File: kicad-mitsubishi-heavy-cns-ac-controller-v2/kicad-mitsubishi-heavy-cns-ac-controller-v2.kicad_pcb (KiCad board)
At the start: 2 copper layers, 42.7 x 48.8 mm, 31 parts, among them J3 USB_OTG, J4 Conn_01x05_Pin, SW1 SW_Push, SW2 SW_Push, U1 Si8641BB-B-IU, U2 AP2112K-3.3, U3 ESP32-C3-WROOM-02, U5 AOZ1282CI-1

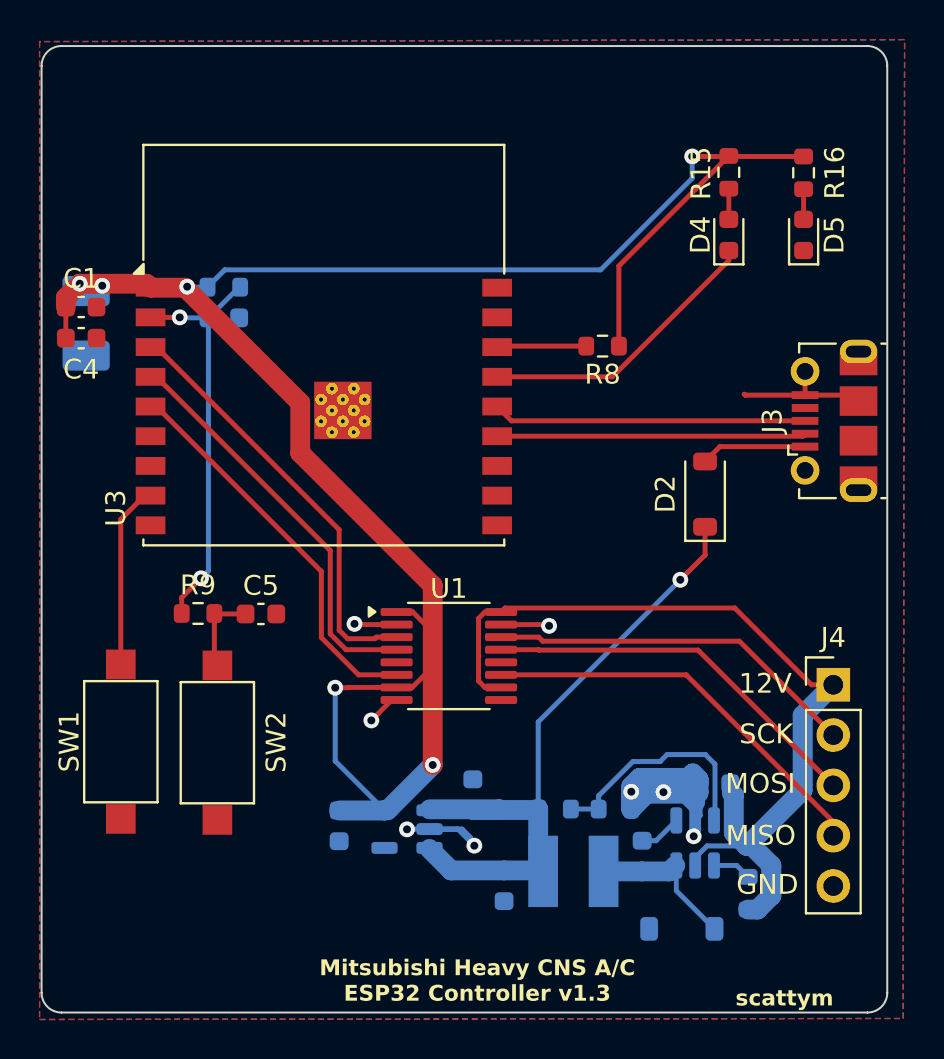
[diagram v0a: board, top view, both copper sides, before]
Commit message: First pcb design for the v2 board.
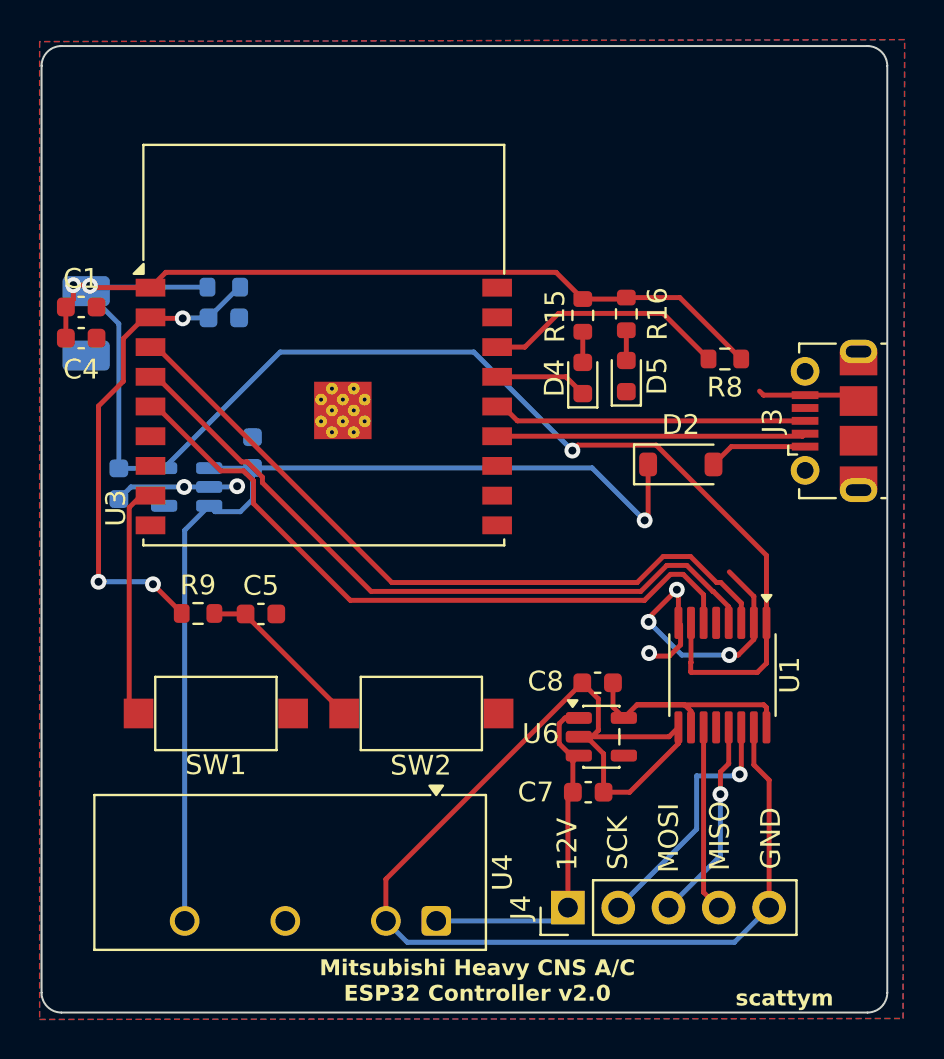
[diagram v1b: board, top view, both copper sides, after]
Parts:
- removed C9: 10uF X7R, Capacitor_SMD:C_0603_1608Metric
- removed D3: PMEG4005EGWX, Diode_SMD:D_SOD-123
- removed L1: 2.2uH, Inductor_SMD:L_Bourns-SRN4018
- removed R12: 49.9K, Resistor_SMD:R_0603_1608Metric
- removed R13: 15.8K, Resistor_SMD:R_0603_1608Metric
- removed R14: 10K, Resistor_SMD:R_0603_1608Metric
- removed U5: AOZ1282CI-1, Package_TO_SOT_SMD:SOT-23-6
- added U4: TBA2-1211, Converter_DCDC:Converter_DCDC_TRACO_TBA2-xxxx_Single_THT, F.Cu at (93.0, 90.2)
- added U6: AP2210K-5.0, Package_TO_SOT_SMD:SOT-23-5, F.Cu at (101.3, 80.9)
- C7: value 10uF X7R -> 1uF X7R; moved to F.Cu
- C8: value 0.1uF -> 2.2uF X7R; moved to F.Cu
- moved C10 20.5 mm to (76.9, 68.1)
- moved C6 20.5 mm to (83.7, 66.5)
- moved U2 20.5 mm to (80.3, 68.3)
- moved J4 17.5 mm to (99.6, 89.5), turned to 90 degrees
- moved U1 13.8 mm to (107.4, 77.8), turned to -90 degrees
- moved D5 11.4 mm to (102.5, 62.7)
- moved R16 11.4 mm to (102.5, 59.5)
- moved SW2 10.4 mm to (92.2, 79.7), turned to 180 degrees
- moved D4 10.3 mm to (100.3, 62.8)
- moved R15 10.3 mm to (100.3, 59.6)
- moved C8 9.03 mm to (101.1, 78.2), turned to 180 degrees
- moved C7 6.41 mm to (100.6, 83.7), turned to 0 degrees
- moved R8 6.21 mm to (107.5, 61.8)
- moved SW1 5.01 mm to (81.8, 79.7), turned to 180 degrees
- moved D2 1.94 mm to (105.3, 67.1), turned to 0 degrees
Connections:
- C1 pad 2: GND -> GND1
- C10 pad 2: GND -> GND1
- C2 pad 2: GND -> GND1
- C3 pad 2: GND -> GND1
- C4 pad 2: GND -> GND1
- C5 pad 2: GND -> GND1
- C6 pad 2: GND -> GND1
- C7 pad 2: GND -> GND2
- C8 pad 1: Net-(U5-BST) -> +5VA
- C8 pad 2: BUCK_PWM_OUT -> GND2
- D5 pad 1: GND -> GND1
- J3 pad 5: GND -> GND1
- J3 pad 6: GND -> GND1
- J4 pad 5: GND -> GND2
- SW1 pad 1: GND -> GND1
- SW2 pad 1: GND -> GND1
- U1 pad 10: +12V -> +5VA
- U1 pad 15: GND -> GND2
- U1 pad 16: +12V -> +5VA
- U1 pad 2: GND -> GND1
- U1 pad 8: GND -> GND1
- U1 pad 9: GND -> GND2
- U2 pad 2: GND -> GND1
- U3 pad 19: GND -> GND1
- U3 pad 9: GND -> GND1
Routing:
- net GND2: track 0.00 -> 64.3 mm
- net +12V: track 61.9 -> 18.2 mm
- net GND: track 42.6 -> 0.00 mm, vias 8 -> 0
- net GND1: track 0.00 -> 28.9 mm, vias 0 -> 6
- net Net-(U1-A1): track 21.5 -> 37.3 mm
- net Net-(U1-A2): track 20.6 -> 36.1 mm
- net Net-(U1-A4): track 20.0 -> 35.0 mm
- net +5V: track 36.9 -> 51.6 mm
- net +5VA: track 0.00 -> 14.2 mm
- net Net-(U5-FB): track 11.9 -> 0.00 mm
- net Net-(J4-Pin_4): track 20.5 -> 9.42 mm
- net LED: track 14.6 -> 4.68 mm
- net BUCK_PWM_OUT: track 9.60 -> 0.00 mm
- net Net-(J4-Pin_3): track 19.6 -> 10.4 mm, vias 0 -> 1
- net Net-(U3-IO2): track 4.52 -> 12.3 mm
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- added copper zone on B.Cu, net GND1
- added copper zone on F.Cu, net GND1
- removed copper zone on B.Cu, net GND
- removed copper zone on F.Cu, net GND
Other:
- board text added: "Mitsubishi Heavy CNS A/C ESP32 Controller v2.0"
- board text removed: "Mitsubishi Heavy CNS A/C ESP32 Controller v1.3"
